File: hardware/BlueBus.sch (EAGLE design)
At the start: 74 parts, among them Y1 32.768kHz

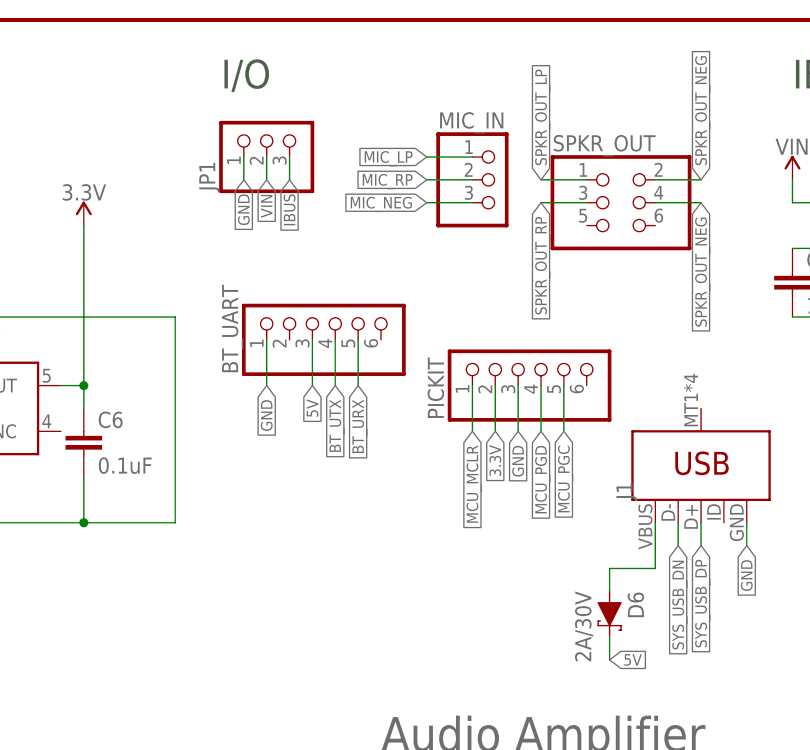
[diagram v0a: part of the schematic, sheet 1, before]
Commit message: [ADD] hardware: Minor board changes * Add mounting holes * Fix uneven pitch of crystal caps * Replace wide through-hole pins with standard sized ones * Update name of TPA6017A2 IC * Update trace widths for 5v rail to .55mm
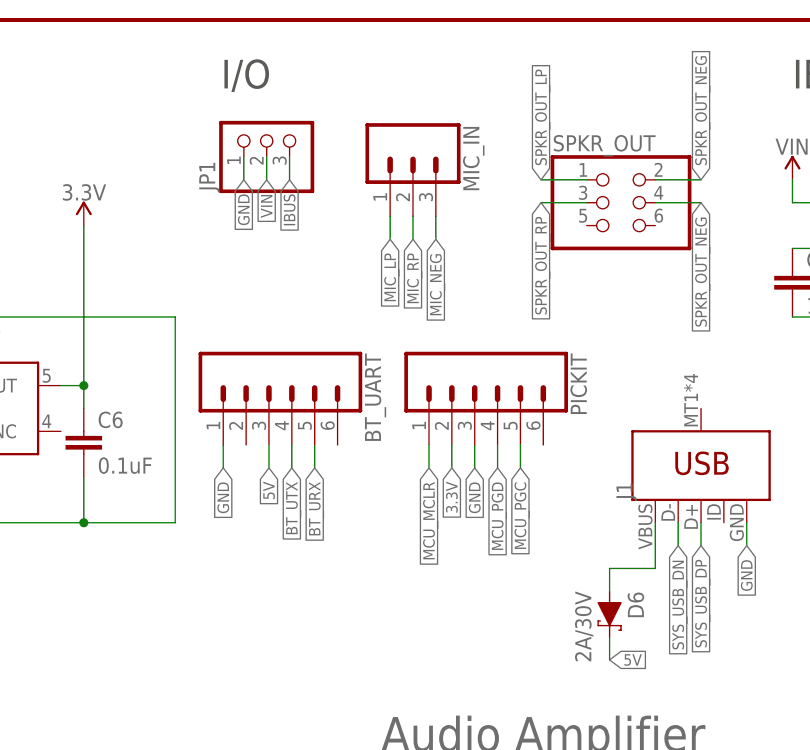
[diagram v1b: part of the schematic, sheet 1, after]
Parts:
- BT_UART, PICKIT: device pinhead:PINHD-1X6 -> SparkFun-Connectors:CONN_06NO_SILK_FEMALE_PTH
- MIC_IN: device pinhead:PINHD-1X3 -> SparkFun-Connectors:CONN_03

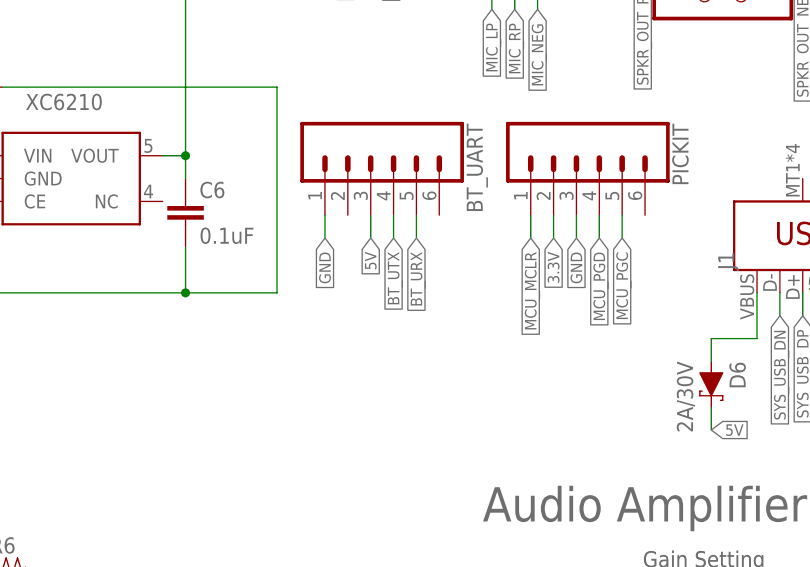
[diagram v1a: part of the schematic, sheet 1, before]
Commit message: [ADD] hardware: BT_UART I/O Change * Re-wire BT_UART for FTDI cable compatability
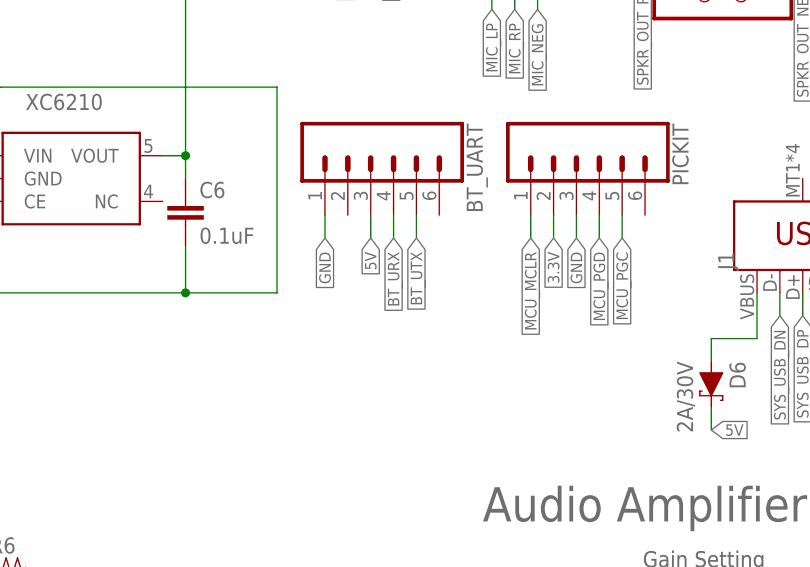
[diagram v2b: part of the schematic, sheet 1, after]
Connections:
- net BT_URX: now also BT_UART.4; no longer BT_UART.5
- net BT_UTX: now also BT_UART.5; no longer BT_UART.4
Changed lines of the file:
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@@
 </segment>
 <segment>
-<pinref part="BT_UART" gate="G$1" pin="4"/>
-<wire x1="122.174" y1="138.176" x2="122.174" y2="135.636" width="0.1524" layer="91"/>
-<label x="122.174" y="135.636" size="1.27" layer="95" rot="R270" xref="yes"/>
+<pinref part="BT_UART" gate="G$1" pin="5"/>
+<wire x1="124.714" y1="138.176" x2="124.714" y2="135.636" width="0.1524" layer="91"/>
+<label x="124.714" y="135.636" size="1.27" layer="95" rot="R270" xref="yes"/>
 </segment>
 </net>
@@
 </segment>
 <segment>
-<pinref part="BT_UART" gate="G$1" pin="5"/>
-<wire x1="124.714" y1="138.176" x2="124.714" y2="135.636" width="0.1524" layer="91"/>
-<label x="124.714" y="135.636" size="1.27" layer="95" rot="R270" xref="yes"/>
+<pinref part="BT_UART" gate="G$1" pin="4"/>
+<wire x1="122.174" y1="138.176" x2="122.174" y2="135.636" width="0.1524" layer="91"/>
+<label x="122.174" y="135.636" size="1.27" layer="95" rot="R270" xref="yes"/>
 </segment>
 </net>

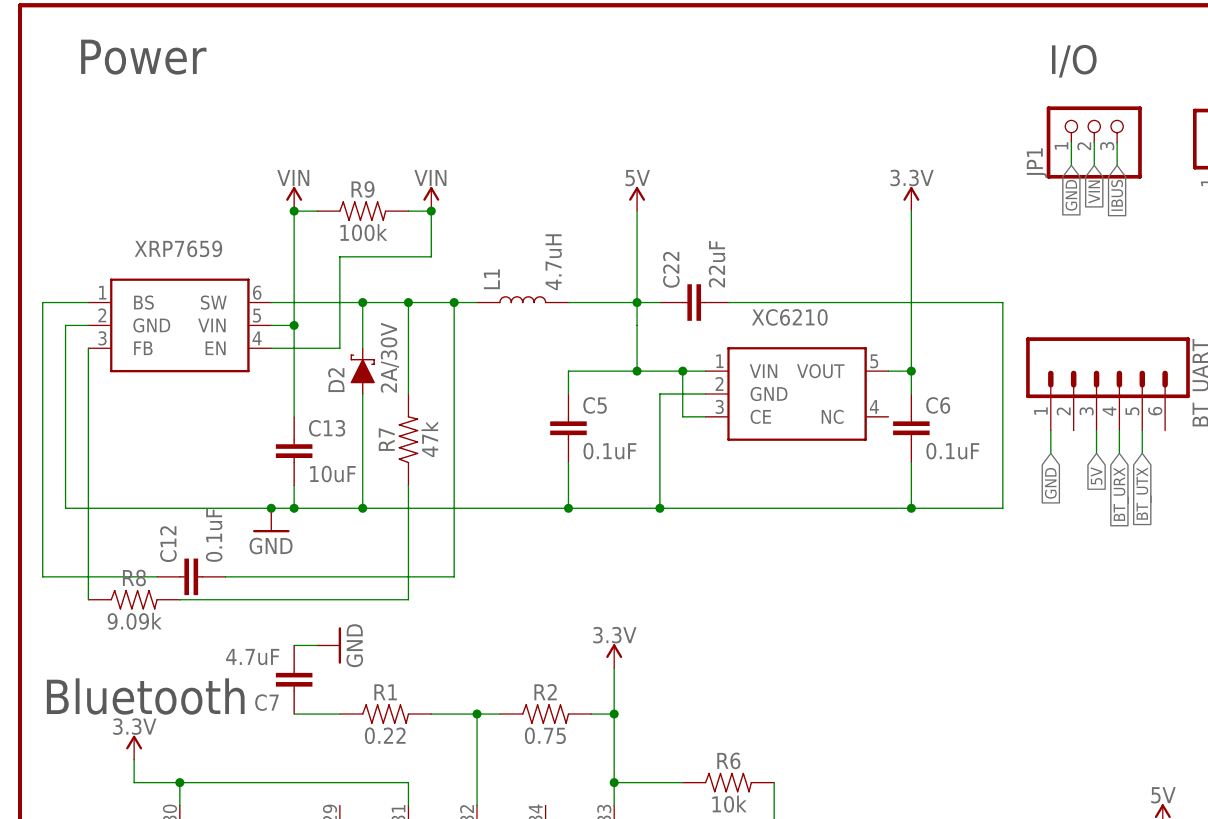
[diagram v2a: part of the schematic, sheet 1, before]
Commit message: [ADD] hardware: Power Management Updates * Wire 5v regulator FB pin to GND * Update BS Cap to 0.01uf from 0.1uf per the datasheet * Add 100kohm resistor to EN pin of 5v regulator * Rewire VIN and 5v Regulator * Update 0.1uF cap on VIN of 3.3v LDO to 1uF per the datasheet * Update 0.1uF cap on VOUT of 3.3v LDO to 2.2uF per the datasheet (>1.0uF required) * Rewire Power Signals so they make more sense
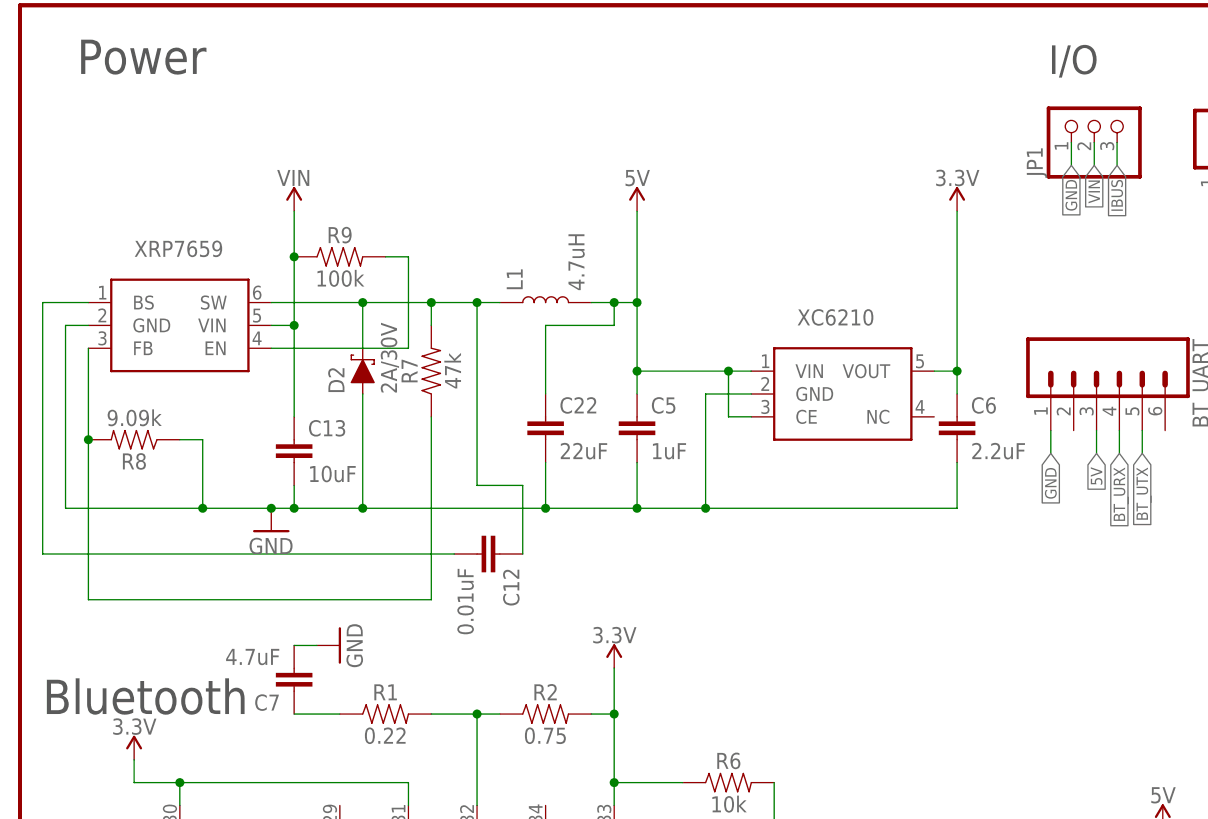
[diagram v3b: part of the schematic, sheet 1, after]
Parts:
- C12: value 0.1uF -> 0.01uF; device Passives:0.1UF -> Passives:0.01UF
- C5: value 0.1uF -> 1uF; device Passives:0.1UF -> Passives:1UF
- C6: value 0.1uF -> 2.2uF; device Passives:0.1UF -> Passives:2.2UF
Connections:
- removed net FB_RES: R7.1, R8.2
- new net EN: R9.2, XRP7659.EN
- net BS: now also C12.2; no longer C12.1
- net FB: now also R7.1, R8.2; no longer R8.1
- net GND: now also R8.1
- net SW: now also C12.1; no longer C12.2
- net VIN: no longer R9.2, XRP7659.EN
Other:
- moved on the sheet: C12, C22, C5, C6, L1, R7, R8, R9

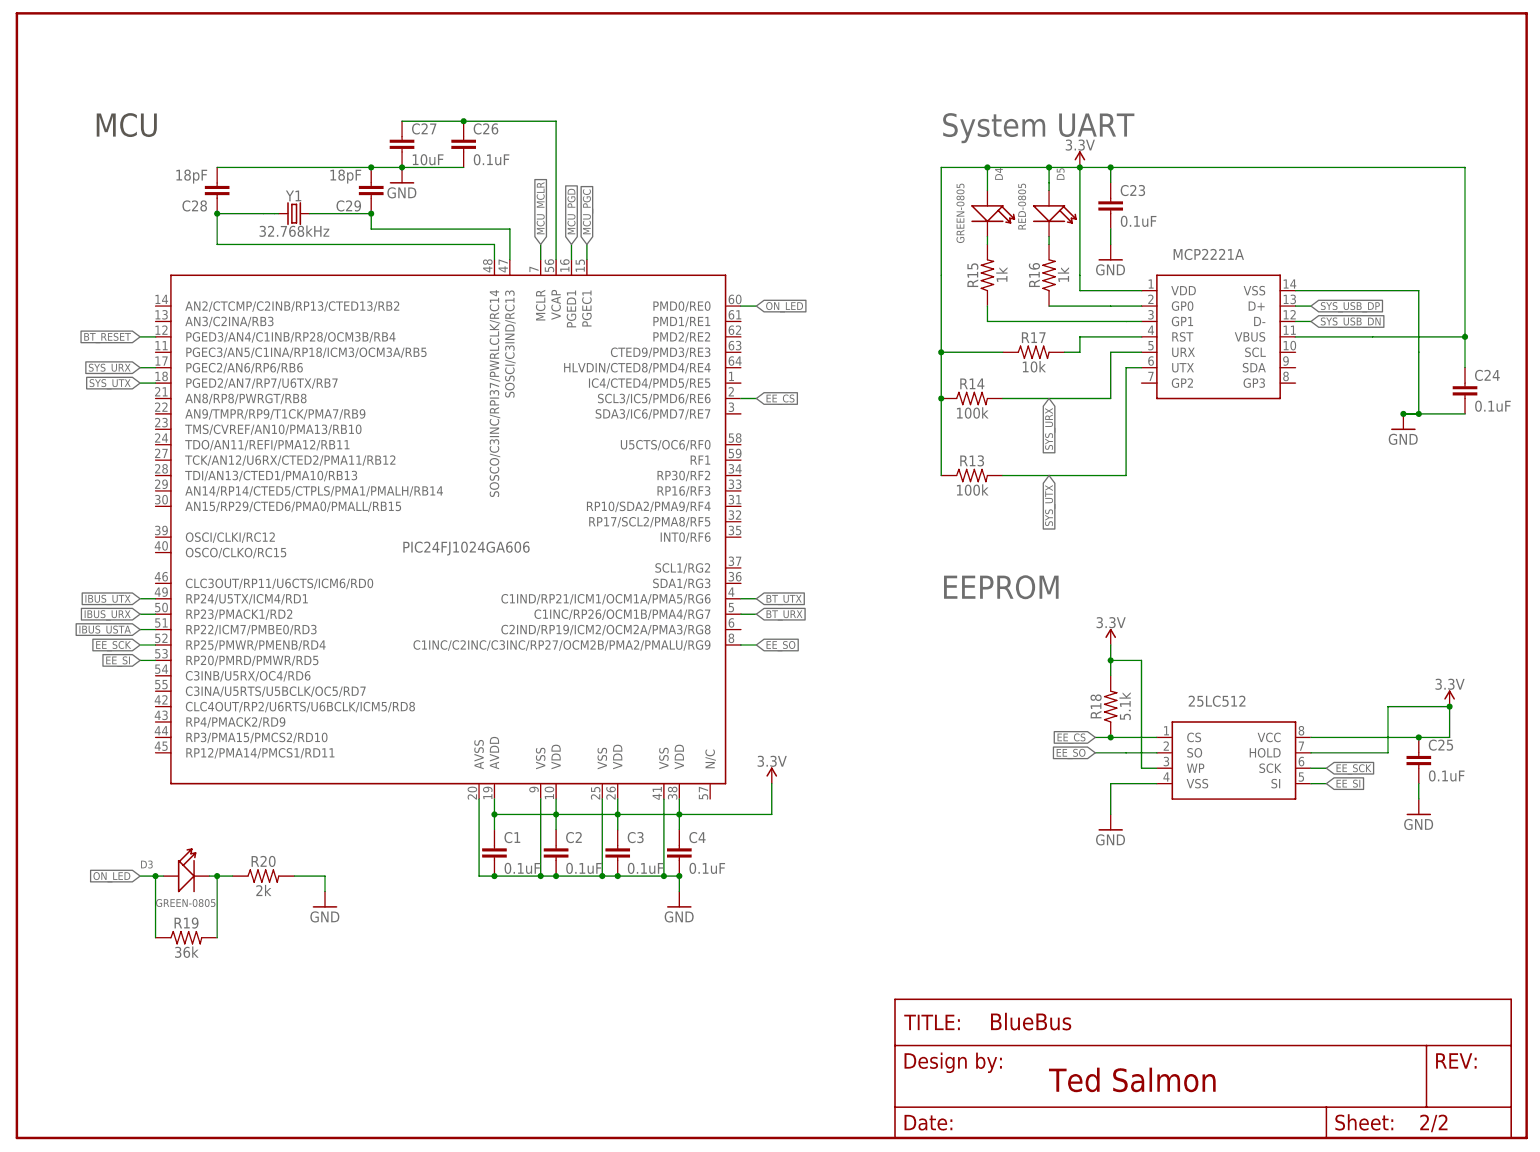
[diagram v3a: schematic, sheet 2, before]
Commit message: [ADD] hardware: BlueBus Board rev. 5 * Add primary 8MHz oscillator * Wire EEPROM signals to compatible pins * Rewire all capacitors so they are not inline with the power rail (Mostly on MCU) * Update pins style to common size instead of the long pin pads * Update size and location of mounting holes * Rewire VIN to make room for mounting holes
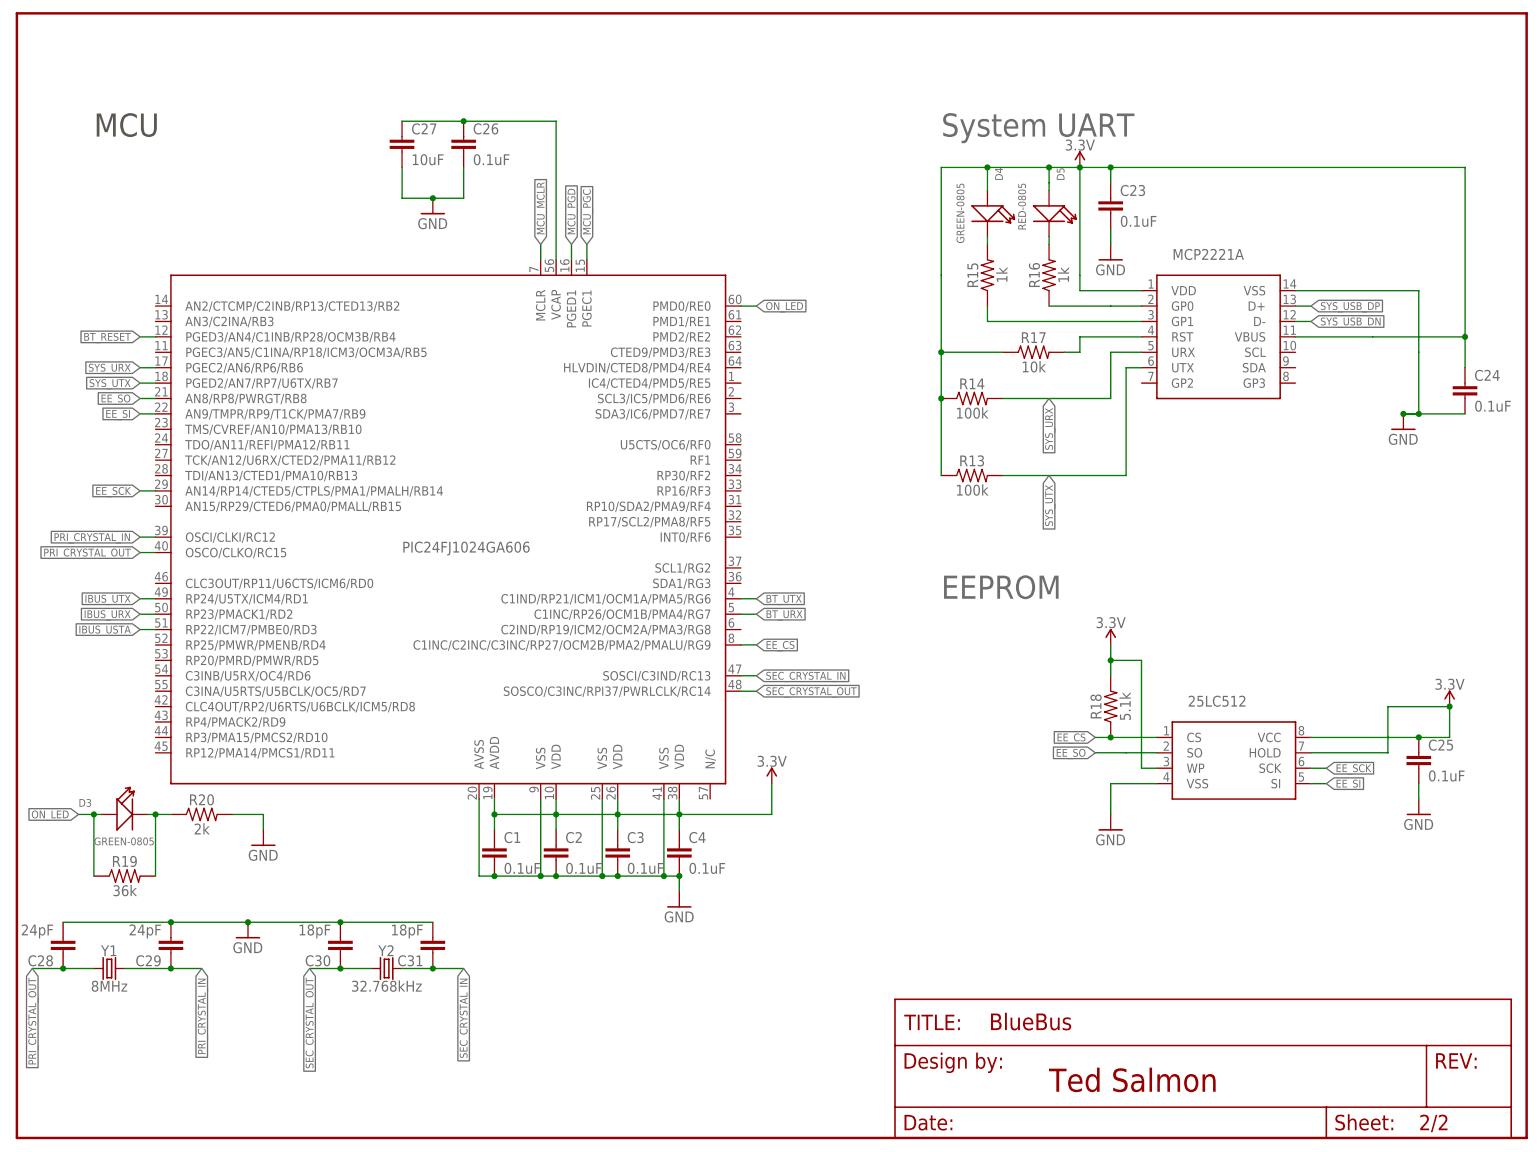
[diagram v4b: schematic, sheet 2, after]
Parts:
- added C30, C31: 18pF, Passives:18PF
- added Y2: 32.768kHz, Passives:CRYSTAL-32.768KHZSMD-3.2X1.5
- BT_UART, PICKIT: device SparkFun-Connectors:CONN_06NO_SILK_FEMALE_PTH -> SparkFun-Connectors:CONN_05
- C28, C29: value 18pF -> 24pF; device Passives:18PF -> Passives:24PF
- Y1: value 32.768kHz -> 8MHz; device Passives:CRYSTAL-32.768KHZSMD-3.2X1.5 -> Passives:CRYSTAL-8MHZ
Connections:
- removed net CRYSTAL_IN: C29.1, PIC24FJ1024GA606.SOSCI/C3IND/RC13, Y1.2
- removed net CRYSTAL_OUT: C28.1, PIC24FJ1024GA606.SOSCO/C3INC/RPI37/PWRLCLK/RC14, Y1.1
- new net PRI_CRYSTAL_IN: C29.1, PIC24FJ1024GA606.OSCI/CLKI/RC12, Y1.2
- new net PRI_CRYSTAL_OUT: C28.1, PIC24FJ1024GA606.OSCO/CLKO/RC15, Y1.1
- new net SEC_CRYSTAL_IN: C31.1, PIC24FJ1024GA606.SOSCI/C3IND/RC13, Y2.2
- new net SEC_CRYSTAL_OUT: C30.1, PIC24FJ1024GA606.SOSCO/C3INC/RPI37/PWRLCLK/RC14, Y2.1
- net EE_CS: now also PIC24FJ1024GA606.C1INC/C2INC/C3INC/RP27/OCM2B/PMA2/PMALU/RG9; no longer PIC24FJ1024GA606.SCL3/IC5/PMD6/RE6
- net EE_SCK: now also PIC24FJ1024GA606.AN14/RP14/CTED5/CTPLS/PMA1/PMALH/RB14; no longer PIC24FJ1024GA606.RP25/PMWR/PMENB/RD4
- net EE_SI: now also PIC24FJ1024GA606.AN9/TMPR/RP9/T1CK/PMA7/RB9; no longer PIC24FJ1024GA606.RP20/PMRD/PMWR/RD5
- net EE_SO: now also PIC24FJ1024GA606.AN8/RP8/PWRGT/RB8; no longer PIC24FJ1024GA606.C1INC/C2INC/C3INC/RP27/OCM2B/PMA2/PMALU/RG9
- net GND: now also C30.2, C31.2
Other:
- moved on the sheet: C28, C29, D3, R19, R20, Y1
